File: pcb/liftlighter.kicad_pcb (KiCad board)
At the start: 2 copper layers, 60 x 90 mm, 54 parts, among them IC1 ATMEGA8-P, P1 CONN_01X06, P12 CONN_01X02, P2 CONN_02X10, P3 CONN_01X02, Q1 BC548, Q10 BC548, Q2 BC548, Q3 BC548, Q4 BC548, Q5 BC548, Q6 BC548, Q7 BC548, Q8 BC548, Q9 BC548, SW1 SW_PUSH, SW2 SW_PUSH, U1 LD1117S33TR, Y1 Crystal

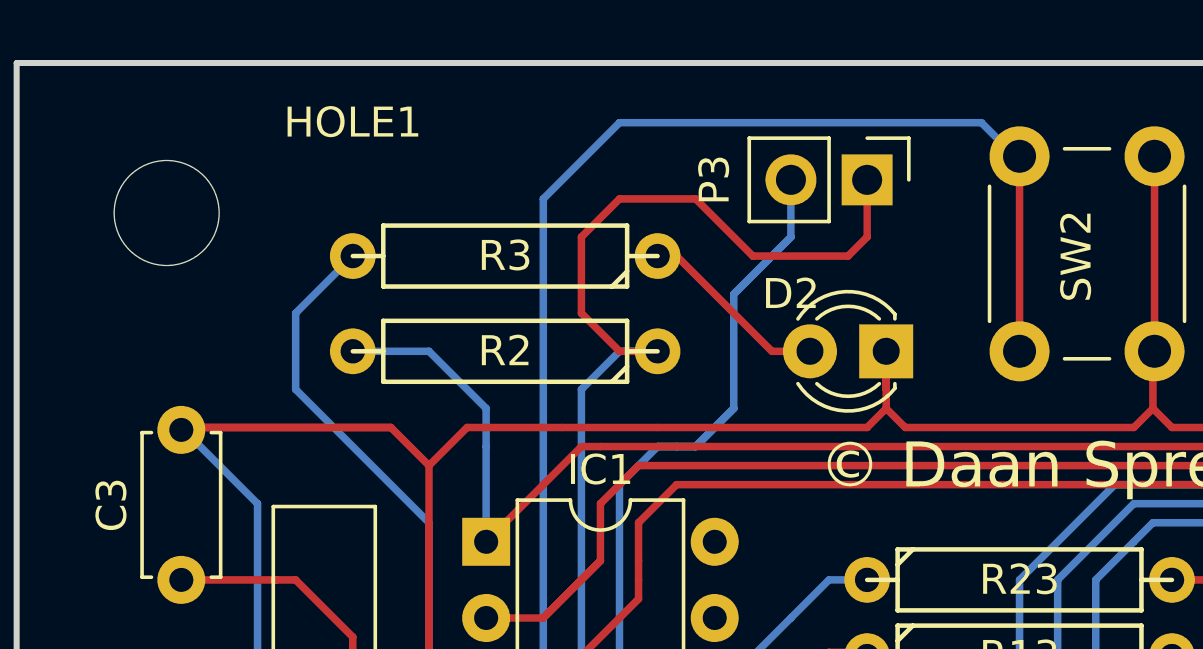
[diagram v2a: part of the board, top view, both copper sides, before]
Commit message: Add pull-down resistor for control button
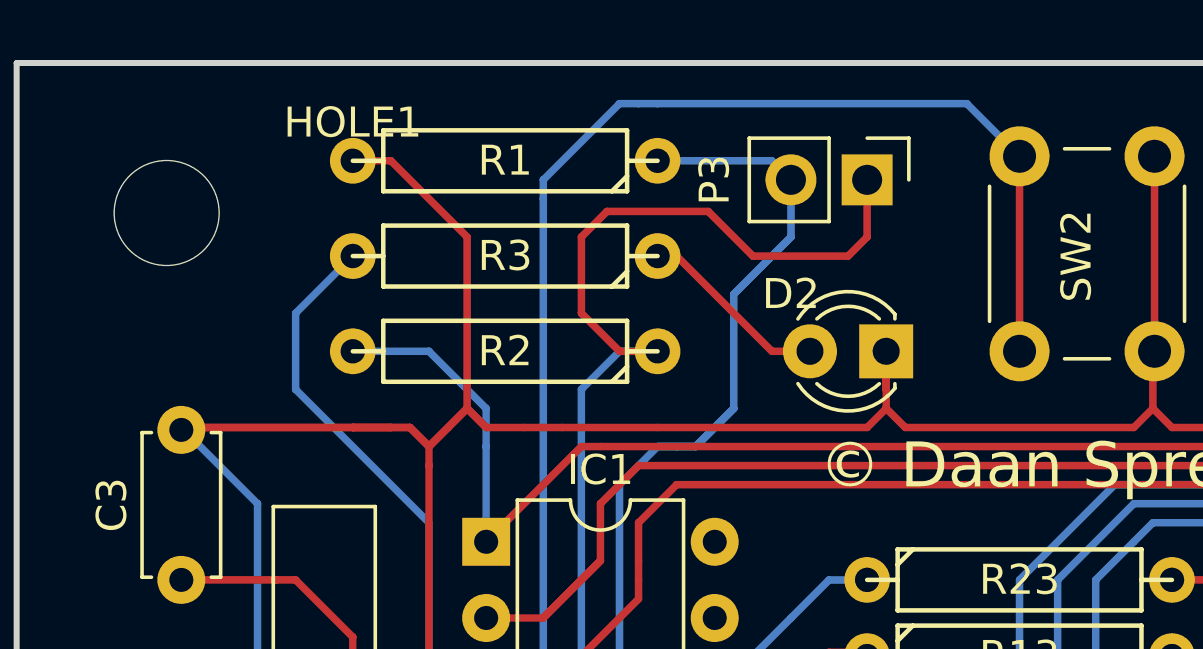
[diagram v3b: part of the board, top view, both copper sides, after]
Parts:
- added R1: R, Discret:R4, F.Cu at (121.3, 48.3)
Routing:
- net GND: track 240.9 -> 257.6 mm
- net Net-(IC1-Pad11): track 50.0 -> 54.7 mm
- net Net-(IC1-Pad4): track 44.5 -> 45.5 mm
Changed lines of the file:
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@@
 (kicad_pcb (version 4) (host pcbnew 4.0.2+dfsg1-stable)
   (general
-    (links 103)
+    (links 105)
     (no_connects 0)
     (area 104.899999 44.899999 165.100001 135.100001)
     (thickness 1.6)
     (drawings 25)
-    (tracks 560)
+    (tracks 577)
     (zones 0)
-    (modules 54)
+    (modules 55)
     (nets 62)
   )
@@
       (net 51 "Net-(P2-Pad20)"))
   )
+  (module Discret:R4 (layer F.Cu)
+    (at 121.285 48.26 180)
+    (descr "Resitance 4 pas")
+    (tags R)
+    (fp_text reference R1 (at 0 0 180) (layer F.SilkS)
+      (effects (font (size 1 1) (thickness 0.15)))
+    )
+    (fp_text value R (at 0 0 180) (layer F.Fab)
+      (effects (font (size 1 1) (thickness 0.15)))
+    )
+    (fp_line (start -5.08 0) (end -4.064 0) (layer F.SilkS) (width 0.15))
+    (fp_line (start -4.064 0) (end -4.064 -1.016) (layer F.SilkS) (width 0.15))
+    (fp_line (start -4.064 -1.016) (end 4.064 -1.016) (layer F.SilkS) (width 0.15))
+    (fp_line (start 4.064 -1.016) (end 4.064 1.016) (layer F.SilkS) (width 0.15))
+    (fp_line (start 4.064 1.016) (end -4.064 1.016) (layer F.SilkS) (width 0.15))
+    (fp_line (start -4.064 1.016) (end -4.064 0) (layer F.SilkS) (width 0.15))
+    (fp_line (start -4.064 -0.508) (end -3.556 -1.016) (layer F.SilkS) (width 0.15))
+    (fp_line (start 5.08 0) (end 4.064 0) (layer F.SilkS) (width 0.15))
+    (pad 1 thru_hole circle (at -5.08 0 180) (size 1.524 1.524) (drill 0.8128) (layers *.Cu *.Mask F.SilkS)
+      (net 33 "Net-(IC1-Pad11)"))
+    (pad 2 thru_hole circle (at 5.08 0 180) (size 1.524 1.524) (drill 0.8128) (layers *.Cu *.Mask F.SilkS)
+      (net 2 GND))
+    (model Discret.3dshapes/R4.wrl
+      (at (xyz 0 0 0))
+      (scale (xyz 0.4 0.4 0.4))
+      (rotate (xyz 0 0 0))
+    )
+  )
   (gr_text - (at 149.86 132.08) (layer F.SilkS)
     (effects (font (size 1.5 1.5) (thickness 0.3)))
@@
   (segment (start 112.395 118.745) (end 112.395 111.125) (width 0.25) (layer F.Cu) (net 1))
   (segment (start 117.475 123.825) (end 112.395 118.745) (width 0.25) (layer F.Cu) (net 1))
+  (segment (start 118.745 58.42) (end 118.745 57.785) (width 0.25) (layer F.Cu) (net 2))
+  (segment (start 119.38 78.74) (end 118.745 78.105) (width 0.25) (layer F.Cu) (net 2))
+  (segment (start 118.745 78.105) (end 118.745 58.42) (width 0.25) (layer F.Cu) (net 2))
+  (segment (start 120.65 78.74) (end 119.38 78.74) (width 0.25) (layer F.Cu) (net 2))
+  (segment (start 121.92 57.15) (end 120.65 57.15) (width 0.25) (layer F.Cu) (net 2))
+  (segment (start 120.65 57.15) (end 120.015 56.515) (width 0.25) (layer F.Cu) (net 2))
+  (segment (start 120.015 56.515) (end 118.745 57.785) (width 0.25) (layer F.Cu) (net 2))
+  (segment (start 118.745 57.785) (end 118.11 57.15) (width 0.25) (layer F.Cu) (net 2))
+  (segment (start 118.11 57.15) (end 116.205 57.15) (width 0.25) (layer F.Cu) (net 2))
+  (segment (start 120.015 56.515) (end 120.65 57.15) (width 0.25) (layer F.Cu) (net 2))
+  (segment (start 117.475 57.15) (end 118.11 57.15) (width 0.25) (layer F.Cu) (net 2))
+  (segment (start 119.38 57.15) (end 120.015 56.515) (width 0.25) (layer F.Cu) (net 2))
+  (segment (start 118.745 57.785) (end 119.38 57.15) (width 0.25) (layer F.Cu) (net 2))
+  (segment (start 118.11 57.15) (end 118.745 57.785) (width 0.25) (layer F.Cu) (net 2))
+  (segment (start 120.015 56.515) (end 120.015 50.8) (width 0.25) (layer F.Cu) (net 2))
+  (segment (start 120.015 50.8) (end 117.475 48.26) (width 0.25) (layer F.Cu) (net 2))
+  (segment (start 117.475 48.26) (end 116.205 48.26) (width 0.25) (layer F.Cu) (net 2))
   (segment (start 146.05 57.15) (end 147.955 57.15) (width 0.25) (layer F.Cu) (net 2))
   (segment (start 148.59 56.515) (end 148.59 54.61) (width 0.25) (layer F.Cu) (net 2))
@@
   (segment (start 110.57 57.23) (end 113.03 59.69) (width 0.25) (layer B.Cu) (net 2))
   (segment (start 110.49 57.23) (end 110.57 57.23) (width 0.25) (layer B.Cu) (net 2))
-  (segment (start 118.745 58.42) (end 117.475 57.15) (width 0.25) (layer F.Cu) (net 2))
+  (segment (start 117.475 57.15) (end 116.205 57.15) (width 0.25) (layer F.Cu) (net 2))
+  (segment (start 116.205 57.15) (end 110.57 57.15) (width 0.25) (layer F.Cu) (net 2))
+  (segment (start 110.57 57.15) (end 110.49 57.23) (width 0.25) (layer F.Cu) (net 2))
   (segment (start 117.475 57.15) (end 110.57 57.15) (width 0.25) (layer F.Cu) (net 2))
   (segment (start 110.57 57.15) (end 110.49 57.23) (width 0.25) (layer F.Cu) (net 2))
-  (segment (start 118.745 58.42) (end 120.015 57.15) (width 0.25) (layer F.Cu) (net 2))
-  (segment (start 120.65 78.74) (end 119.38 78.74) (width 0.25) (layer F.Cu) (net 2))
-  (segment (start 118.745 78.105) (end 118.745 58.42) (width 0.25) (layer F.Cu) (net 2))
-  (segment (start 119.38 78.74) (end 118.745 78.105) (width 0.25) (layer F.Cu) (net 2))
-  (segment (start 117.475 57.15) (end 110.57 57.15) (width 0.25) (layer F.Cu) (net 2))
-  (segment (start 110.57 57.15) (end 110.49 57.23) (width 0.25) (layer F.Cu) (net 2))
-  (segment (start 120.65 57.15) (end 123.19 57.15) (width 0.25) (layer F.Cu) (net 2))
+  (segment (start 121.92 57.15) (end 123.19 57.15) (width 0.25) (layer F.Cu) (net 2))
+  (segment (start 133.985 56.515) (end 133.35 57.15) (width 0.25) (layer F.Cu) (net 2))
+  (segment (start 133.35 57.15) (end 126.365 57.15) (width 0.25) (layer F.Cu) (net 2))
   (segment (start 126.365 57.15) (end 123.19 57.15) (width 0.25) (layer F.Cu) (net 2))
-  (segment (start 133.35 57.15) (end 126.365 57.15) (width 0.25) (layer F.Cu) (net 2))
-  (segment (start 133.985 56.515) (end 133.35 57.15) (width 0.25) (layer F.Cu) (net 2))
-  (segment (start 120.015 57.15) (end 120.65 57.15) (width 0.25) (layer F.Cu) (net 2))
   (segment (start 133.985 55.88) (end 133.985 54.61) (width 0.25) (layer F.Cu) (net 2))
   (segment (start 133.985 56.515) (end 134.62 57.15) (width 0.25) (layer F.Cu) (net 2))
@@
   (segment (start 113.03 96.52) (end 110.49 96.52) (width 0.5) (layer F.Cu) (net 3))
   (segment (start 115.57 93.98) (end 113.03 96.52) (width 0.5) (layer F.Cu) (net 3))
+  (segment (start 128.0525 49.9475) (end 124.6775 49.9475) (width 0.25) (layer F.Cu) (net 4))
   (segment (start 128.27 114.3) (end 128.27 113.03) (width 0.25) (layer F.Cu) (net 4))
   (segment (start 125.73 110.49) (end 125.73 100.33) (width 0.25) (layer F.Cu) (net 4))
   (segment (start 128.27 113.03) (end 125.73 110.49) (width 0.25) (layer F.Cu) (net 4))
   (segment (start 128.27 127) (end 128.27 114.3) (width 0.25) (layer F.Cu) (net 4))
-  (segment (start 127.635 49.53) (end 125.095 49.53) (width 0.25) (layer F.Cu) (net 4))
   (segment (start 122.555 76.2) (end 123.825 74.93) (width 0.25) (layer B.Cu) (net 4))
   (segment (start 123.825 74.93) (end 123.825 55.88) (width 0.25) (layer B.Cu) (net 4))
@@
   (segment (start 133.35 50.8) (end 132.715 51.435) (width 0.25) (layer F.Cu) (net 4))
   (segment (start 132.715 51.435) (end 129.54 51.435) (width 0.25) (layer F.Cu) (net 4))
-  (segment (start 129.54 51.435) (end 127.635 49.53) (width 0.25) (layer F.Cu) (net 4))
-  (segment (start 125.095 49.53) (end 123.825 50.8) (width 0.25) (layer F.Cu) (net 4))
+  (segment (start 129.54 51.435) (end 128.0525 49.9475) (width 0.25) (layer F.Cu) (net 4))
+  (segment (start 124.6775 49.9475) (end 123.825 50.8) (width 0.25) (layer F.Cu) (net 4))
   (segment (start 123.825 50.8) (end 123.825 53.34) (width 0.25) (layer F.Cu) (net 4))
   (segment (start 123.825 53.34) (end 125.095 54.61) (width 0.25) (layer F.Cu) (net 4))
@@
   (segment (start 148.59 71.12) (end 147.32 69.85) (width 0.5) (layer B.Cu) (net 30))
   (segment (start 147.32 66.04) (end 148.59 64.77) (width 0.5) (layer B.Cu) (net 30))
+  (segment (start 122.555 48.895) (end 125.095 46.355) (width 0.25) (layer B.Cu) (net 31))
+  (segment (start 125.095 46.355) (end 125.73 46.355) (width 0.25) (layer B.Cu) (net 31))
+  (segment (start 126.365 46.355) (end 125.73 46.355) (width 0.25) (layer B.Cu) (net 31))
+  (segment (start 126.365 46.355) (end 136.675 46.355) (width 0.25) (layer B.Cu) (net 31))
+  (segment (start 136.675 46.355) (end 138.43 48.11) (width 0.25) (layer B.Cu) (net 31))
+  (segment (start 122.555 48.895) (end 122.555 49.53) (width 0.25) (layer B.Cu) (net 31))
   (segment (start 138.43 48.11) (end 138.28 48.11) (width 0.25) (layer B.Cu) (net 31))
-  (segment (start 138.28 48.11) (end 137.16 46.99) (width 0.25) (layer B.Cu) (net 31))
-  (segment (start 137.16 46.99) (end 125.095 46.99) (width 0.25) (layer B.Cu) (net 31))
   (segment (start 121.92 68.58) (end 120.65 68.58) (width 0.25) (layer B.Cu) (net 31))
+  (segment (start 122.555 49.53) (end 122.555 67.945) (width 0.25) (layer B.Cu) (net 31))
   (segment (start 122.555 67.945) (end 121.92 68.58) (width 0.25) (layer B.Cu) (net 31))
-  (segment (start 122.555 49.53) (end 122.555 67.945) (width 0.25) (layer B.Cu) (net 31))
-  (segment (start 125.095 46.99) (end 122.555 49.53) (width 0.25) (layer B.Cu) (net 31))
   (segment (start 138.43 54.61) (end 138.43 48.11) (width 0.25) (layer F.Cu) (net 31))
   (segment (start 120.65 73.66) (end 120.015 73.66) (width 0.25) (layer B.Cu) (net 32))
@@
   (segment (start 114.3 53.34) (end 114.3 55.88) (width 0.25) (layer B.Cu) (net 32))
   (segment (start 116.205 51.435) (end 114.3 53.34) (width 0.25) (layer B.Cu) (net 32))
+  (segment (start 126.365 48.26) (end 130.175 48.26) (width 0.25) (layer B.Cu) (net 33))
+  (segment (start 130.175 48.26) (end 130.81 48.895) (width 0.25) (layer B.Cu) (net 33))
   (segment (start 128.905 52.705) (end 128.905 56.515) (width 0.25) (layer B.Cu) (net 33))
   (segment (start 130.81 48.895) (end 130.81 50.8) (width 0.25) (layer B.Cu) (net 33))
